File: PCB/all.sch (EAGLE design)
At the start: 122 parts, among them J1 ISP Programmer, J2 LIPO-BATTERY-CONNECTOR, J8 BL-HP20AUW2C, U1 ATTINY1634MLF20, U2 LM3671, U3 MPU-6050-1, U4 BQ51013B_RHL_20, U5 MCP73831, U6 CAT4139, U7 BQ51013B_RHL_20, U8 BQ51013B_RHL_20, U9 BQ51013B_RHL_20

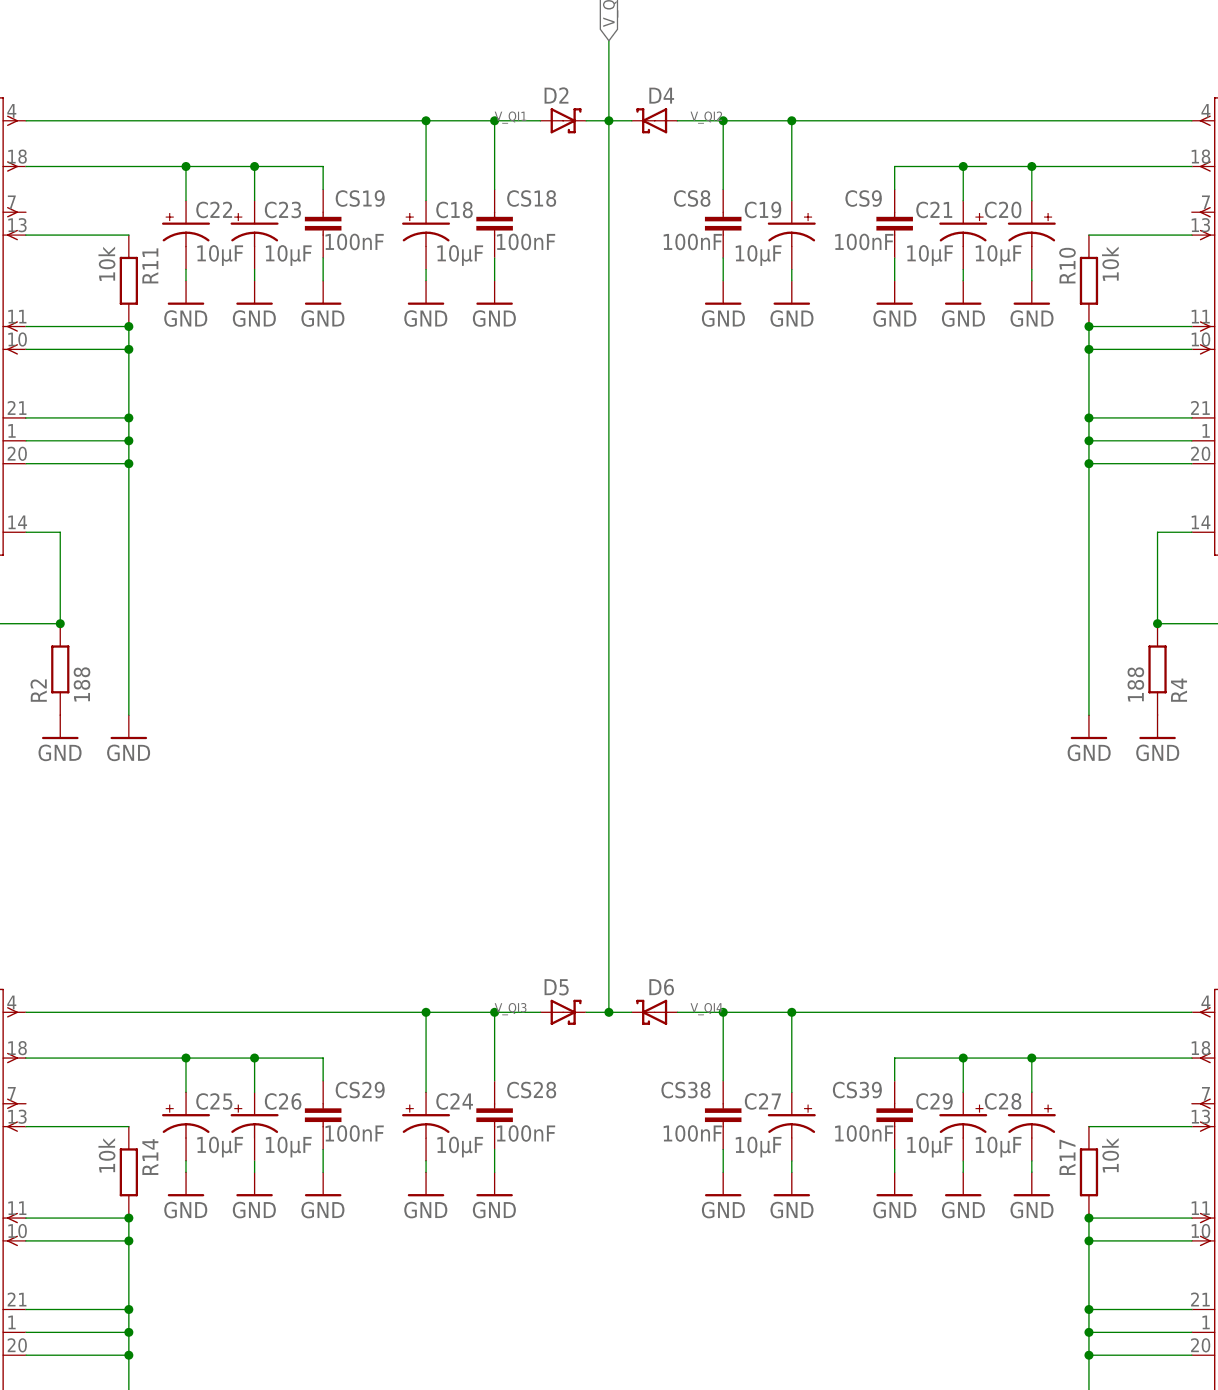
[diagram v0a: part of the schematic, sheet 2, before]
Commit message: rerouted Qi chargers and finished arrangements
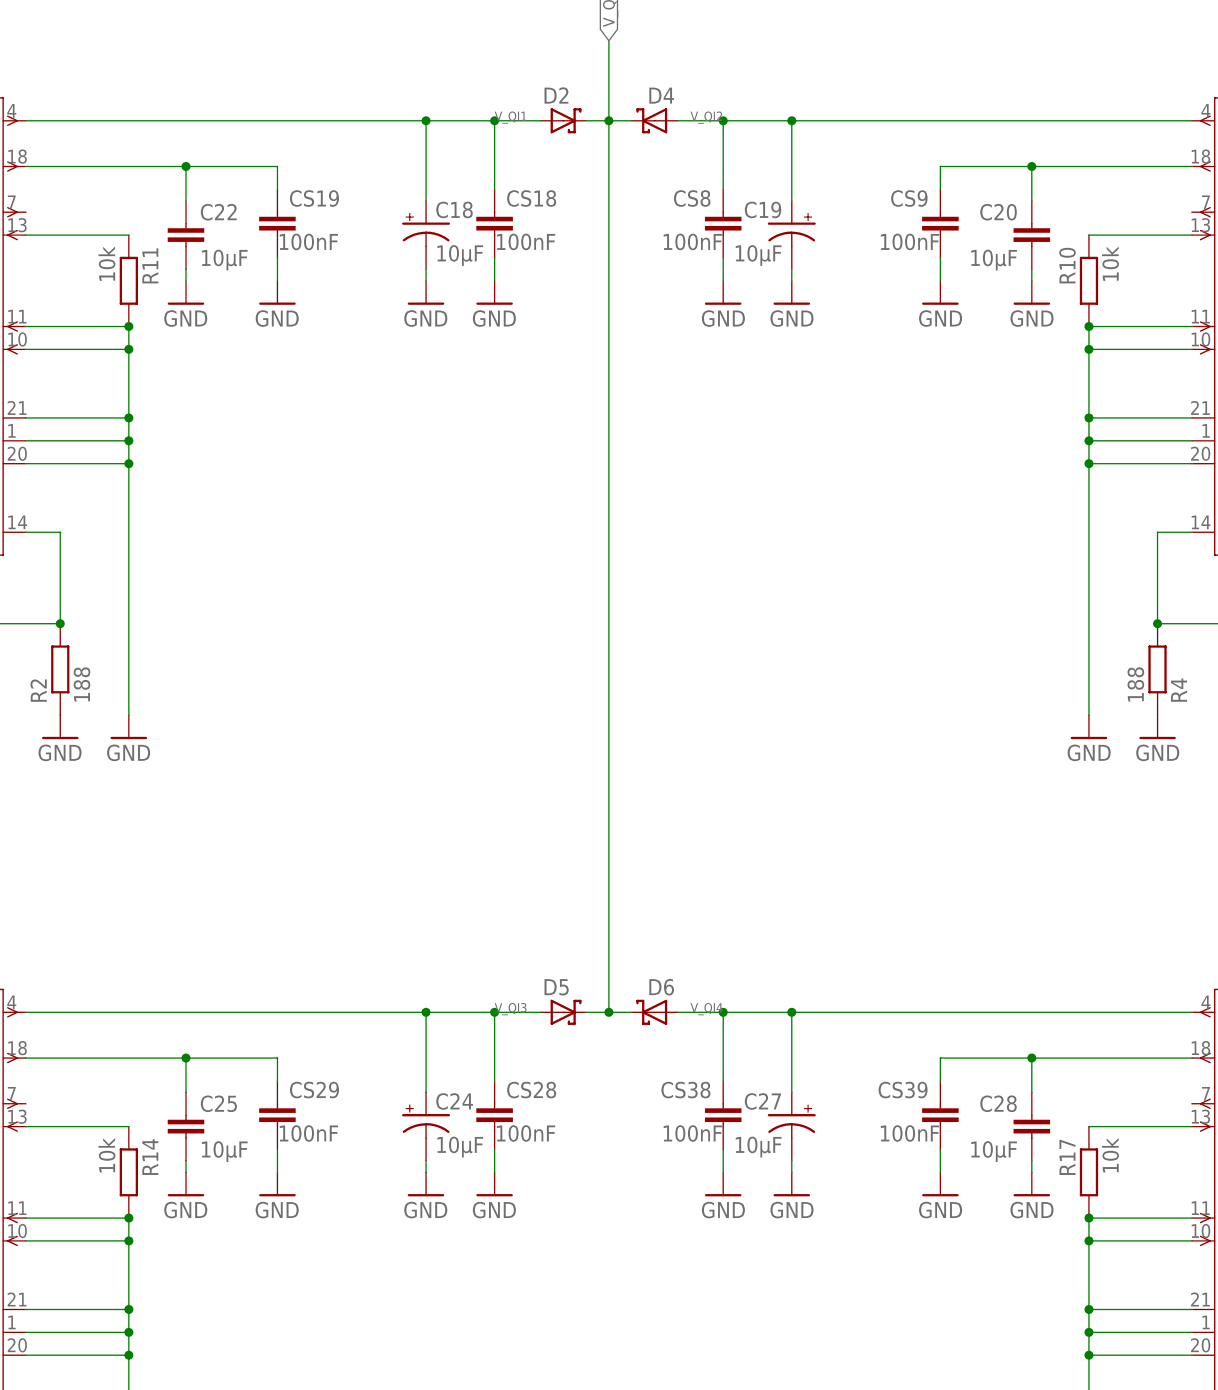
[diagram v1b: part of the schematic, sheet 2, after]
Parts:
- removed C21, C23, C26, C29: 10μF, SparkFun:CAP_POL1206
- C20, C22, C25, C28: device SparkFun:CAP_POL1206 -> rcl:C-EUC0603
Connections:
- net GND: now also C20.2, C22.2, C25.2, C28.2; no longer C20.-, C21.-, C22.-, C23.-, C25.-, C26.-, C28.-, C29.-
- net N$23: now also C20.1; no longer C20.+, C21.+
- net N$32: now also C22.1; no longer C22.+, C23.+
- net N$45: now also C25.1; no longer C25.+, C26.+
- net N$58: now also C28.1; no longer C28.+, C29.+
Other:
- note removed: "Battery charger: MCP73831 ---------------------- for charging current of 100 mA, R6 is 10k"
- moved on the sheet: CS19, CS29, CS39, CS9

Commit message: routing finished
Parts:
- C1, C17, C20, C22, C25, C28, C5, CP1, CP2, CP3, CP4, CP5, CP6, CP7, CP8, CS, CS1, CS10, CS11, CS12, CS13, CS14, CS15, CS16, CS17, CS19, CS2, CS20, CS21, CS22, CS23, CS24, CS25, CS26, CS27, CS28, CS29, CS3, CS30, CS31, CS32, CS33, CS34, CS35, CS36, CS37, CS38, CS39, CS4, CS5, CS6, CS7, CS8, CS9: device rcl:C-EUC0603 -> rcl:C-EUC0603K
- C10, C11, C12, C6, C7, C8, C9: device rcl:C-EUC0402 -> rcl:C-EUC0603K
- C13: device SparkFun:CAP0603-CAP -> rcl:C-EUC0603K
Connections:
- removed net VBAT: J2.+, U5.VBAT
- net 5V: now also J2.+
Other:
- moved on the sheet: C13

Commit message: DRC done
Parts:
- J3, J4, J5, J6: value (none) -> Qi coil
- J7: value (none) -> UART
- Q1, Q2: value (none) -> NPN
- R18: value (none) -> 1.8
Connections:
- removed net 5V: C1.1, C14.+, C8.1, J1.2, J2.+, JP2.2, L1.1, SJ2.3, U2.EN, U2.IN, U6.VIN
- new net +5V: C1.1, C14.+, C8.1, J1.2, J2.+, JP2.2, L1.1, SJ2.3, U2.EN, U2.IN, U5.VBAT, U6.VIN

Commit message: fabrication output generated
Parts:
- added FD1, FD2: FIDUCIAL1X2, SparkFun-Aesthetics:FIDUCIAL1X2
- SJ1, SJ2: value (none) -> JUMPER-PAD-3-2OF3_NC_BY_TRACE_SMALL; device SparkFun-Retired:SOLDERJUMPER_2WAYPASTE2&3 -> SparkFun-Passives:JUMPER-PAD-3-2OF3_NC_BY_TRACE_SMALL
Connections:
- net +5V: now also SJ2.1; no longer SJ2.3
- net N$3: now also SJ1.1; no longer SJ1.3
- net N$4: now also SJ1.3; no longer SJ1.1
- net N$64: now also SJ2.3; no longer SJ2.1
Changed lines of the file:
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@@
 <part name="R18" library="rcl" deviceset="R-EU_" device="R0603" value="1.8"/>
 <part name="GND3" library="SparkFun" deviceset="GND" device=""/>
-<part name="SJ1" library="SparkFun-Retired" deviceset="SOLDERJUMPER_2WAY" device="PASTE2&amp;3"/>
+<part name="SJ1" library="SparkFun-Passives" deviceset="JUMPER-PAD-3-2OF3_NC_BY_TRACE" device="_SMALL" value=""/>
 <part name="U6" library="pero_library" deviceset="CAT4139" device="" value="CAT4139"/>
 <part name="C1" library="rcl" deviceset="C-EU" device="C0603K" value="10μF"/>
@@
 <part name="GND29" library="SparkFun" deviceset="GND" device=""/>
 <part name="R20" library="resistor" deviceset="R-EU_" device="R0603" value="1k"/>
-<part name="SJ2" library="SparkFun-Retired" deviceset="SOLDERJUMPER_2WAY" device="PASTE2&amp;3"/>
+<part name="SJ2" library="SparkFun-Passives" deviceset="JUMPER-PAD-3-2OF3_NC_BY_TRACE" device="_SMALL" value=""/>
 <part name="FRAME3" library="frames" deviceset="A4L-LOC" device=""/>
 <part name="L2" library="SparkFun-Passives" deviceset="INDUCTOR" device="SDR0403-560KL" value="22uH"/>
@@
 <part name="P+5" library="supply1" deviceset="+5V" device=""/>
 <part name="U5" library="SparkFun-PowerIC" deviceset="MCP73831" device=""/>
+<part name="FD1" library="SparkFun-Aesthetics" deviceset="FIDUCIAL" device="1X2"/>
+<part name="FD2" library="SparkFun-Aesthetics" deviceset="FIDUCIAL" device="1X2"/>
 </parts>
 <sheets>
@@
 <instance part="R18" gate="G$1" x="226.06" y="76.2" rot="R90"/>
 <instance part="GND3" gate="1" x="226.06" y="66.04"/>
-<instance part="SJ1" gate="G$1" x="213.36" y="96.52"/>
+<instance part="SJ1" gate="G$1" x="213.36" y="96.52" rot="MR180"/>
 <instance part="U6" gate="G$1" x="185.42" y="127" smashed="yes">
 <attribute name="NAME" x="175.26" y="134.62" size="1.778" layer="95"/>
@@
 <instance part="GND29" gate="1" x="218.44" y="109.22"/>
 <instance part="R20" gate="G$1" x="208.28" y="121.92"/>
-<instance part="SJ2" gate="G$1" x="220.98" y="139.7" rot="R90"/>
+<instance part="SJ2" gate="G$1" x="220.98" y="139.7" smashed="yes" rot="MR90">
+<attribute name="NAME" x="220.98" y="142.621" size="1.778" layer="95" rot="MR0"/>
+<attribute name="VALUE" x="219.075" y="142.24" size="1.778" layer="96" rot="MR90"/>
+</instance>
 <instance part="FRAME3" gate="G$1" x="0" y="0"/>
 <instance part="L2" gate="G$1" x="130.81" y="153.67" smashed="yes" rot="R90">
 <attribute name="NAME" x="128.27" y="158.242" size="1.778" layer="95" rot="R180"/>
 </instance>
-<instance part="P+1" gate="1" x="92.71" y="158.75"/>
-<instance part="P+2" gate="1" x="226.06" y="144.78"/>
-<instance part="P+3" gate="1" x="162.56" y="144.526"/>
-<instance part="P+4" gate="1" x="162.56" y="65.786"/>
-<instance part="P+5" gate="1" x="101.6" y="121.92"/>
+<instance part="P+1" gate="1" x="92.71" y="158.75" smashed="yes">
+<attribute name="VALUE" x="95.25" y="161.29" size="1.778" layer="96" rot="R180"/>
+</instance>
+<instance part="P+2" gate="1" x="226.06" y="144.78" smashed="yes">
+<attribute name="VALUE" x="228.6" y="147.32" size="1.778" layer="96" rot="R180"/>
+</instance>
+<instance part="P+3" gate="1" x="162.56" y="144.526" smashed="yes">
+<attribute name="VALUE" x="165.354" y="147.32" size="1.778" layer="96" rot="R180"/>
+</instance>
+<instance part="P+4" gate="1" x="162.56" y="65.786" smashed="yes">
+<attribute name="VALUE" x="165.354" y="68.58" size="1.778" layer="96" rot="R180"/>
+</instance>
+<instance part="P+5" gate="1" x="101.6" y="121.92" smashed="yes">
+<attribute name="VALUE" x="104.14" y="124.46" size="1.778" layer="96" rot="R180"/>
+</instance>
 <instance part="U5" gate="G$1" x="46.99" y="151.13"/>
+<instance part="FD1" gate="G$1" x="215.9" y="43.18"/>
+<instance part="FD2" gate="G$1" x="226.06" y="43.18"/>
 </instances>
 <busses>
@@
 </segment>
 </net>
-<net name="N$3" class="0">
-<segment>
-<pinref part="Q1" gate="G$1" pin="B"/>
-<pinref part="Q2" gate="G$1" pin="C"/>
-<wire x1="220.98" y1="91.44" x2="213.36" y2="91.44" width="0.1524" layer="91"/>
-<wire x1="213.36" y1="91.44" x2="213.36" y2="88.9" width="0.1524" layer="91"/>
-<pinref part="SJ1" gate="G$1" pin="3"/>
-<junction x="213.36" y="91.44"/>
-</segment>
-</net>
 <net name="N$63" class="0">
 <segment>
@@
 <wire x1="208.28" y1="139.7" x2="210.82" y2="139.7" width="0.1524" layer="91"/>
 <pinref part="C17" gate="G$1" pin="1"/>
-<pinref part="SJ2" gate="G$1" pin="1"/>
+<pinref part="SJ2" gate="G$1" pin="3"/>
 <wire x1="210.82" y1="139.7" x2="215.9" y2="139.7" width="0.1524" layer="91"/>
 <junction x="210.82" y="139.7"/>
@@
 <pinref part="U6" gate="G$1" pin="SHDN"/>
 <wire x1="170.18" y1="121.92" x2="170.18" y2="101.6" width="0.1524" layer="91"/>
-<pinref part="SJ1" gate="G$1" pin="1"/>
+<pinref part="SJ1" gate="G$1" pin="3"/>
 <wire x1="170.18" y1="101.6" x2="213.36" y2="101.6" width="0.1524" layer="91"/>
 </segment>
@@
 </segment>
 <segment>
-<pinref part="SJ2" gate="G$1" pin="3"/>
-<wire x1="226.06" y1="139.7" x2="226.06" y2="142.24" width="0.1524" layer="91"/>
-<pinref part="P+2" gate="1" pin="+5V"/>
-</segment>
-<segment>
 <pinref part="C1" gate="G$1" pin="1"/>
 <wire x1="162.56" y1="129.54" x2="162.56" y2="139.7" width="0.1524" layer="91"/>
@@
 <pinref part="P+5" gate="1" pin="+5V"/>
 </segment>
-</net>
+<segment>
+<pinref part="SJ2" gate="G$1" pin="1"/>
+<pinref part="P+2" gate="1" pin="+5V"/>
+<wire x1="226.06" y1="139.7" x2="226.06" y2="142.24" width="0.1524" layer="91"/>
+</segment>
+</net>
+<net name="N$3" class="0">
+<segment>
+<pinref part="SJ1" gate="G$1" pin="1"/>
+<pinref part="Q2" gate="G$1" pin="C"/>
+<wire x1="213.36" y1="91.44" x2="213.36" y2="88.9" width="0.1524" layer="91"/>
+<pinref part="Q1" gate="G$1" pin="B"/>
+<wire x1="220.98" y1="91.44" x2="213.36" y2="91.44" width="0.1524" layer="91"/>
+<junction x="213.36" y="91.44"/>
+</segment>
+</net>

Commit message: going back to 32u4
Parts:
- removed J7: UART, SparkFun-Connectors:M02PTH
- removed R1: 10k, rcl:R-EU_R0603
- added C2: 1µF, rcl:C-EUC0603
- added C23, C3: 18p, rcl:C-EUC0603
- added F2: PTC0603, SparkFun-PowerIC:PTC0603
- added Q3: 8MHz, pero_library:QUARTZ-CRYSTAL-8MHZQC6CB8.00000F18B23R
- added R21: 10k, rcl:R-EU_R0603
- added R23, R24: 22, rcl:R-EU_R0603
- added S1: Reset, pero_library:SWITCH-BUTTON-SKSGAAE010
- J1: value ISP Programmer -> micro USB; device SparkFun:AVR_SPI_PRG_6PTH -> SparkFun-Connectors:USB_MICROB_PLUGCONN-11752
- L2: value 22uH -> 2.2uH
- U1: value ATTINY1634MLF20 -> ATMEGA32U4QFN; device attiny1634:ATTINY1634MLF20 -> SparkFun-DigitalIC:ATMEGA32U4QFN
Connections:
- removed net MISO: J1.1, U1.ADC7/MISO/TXD1/DO/PB2
- removed net RX: J7.1, U1.PA7/RXD0/ADC4
- removed net TX: J7.2, U1.PB0/TXD0/ADC5
- new net N$71: C23.2, Q3.2, U1.XTAL1
- new net N$72: C3.2, Q3.1, U1.XTAL2
- new net N$73: F2.1, J1.VCC
- new net N$74: J1.D+, R23.1
- new net N$78: J1.D-, R24.1
- new net N$80: R23.2, U1.D+
- new net N$81: R24.2, U1.D-
- new net VUSB: F2.2, U1.VBUS
- net +5V: no longer J1.2
- net 3.3V: now also C2.1, R21.2, U1.AVCC@24, U1.AVCC@44, U1.UCAP, U1.VCC@14, U1.VCC@34; no longer R1.2, U1.VCC
- net GND: now also C2.2, C23.1, C3.1, J1.GND, S1.1, U1.GND@15, U1.GND@23, U1.GND@35, U1.GND@43, U1.UGND; no longer J1.6, U1.GND
- net PWM: no longer U1.ADC9/OC0A/XCK0/PC0
- net RGB: no longer U1.PA6/ADC3/OC1B
- net RST: now also R21.1, S1.2, U1.!RESET; no longer J1.5, R1.1, U1.-RESET/PC3
- net SCL: now also U1.PD0(SCL); no longer J1.3, U1.ADC10/SCL/USCK/XCK1/PC1
- net SDA: now also U1.PD1(SDA); no longer J1.4, U1.RXD1/ADC6/DI/SDA/MOSI/PB1
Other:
- moved on the sheet: C1, C10, C11, C12, C13, C14, C15, C17, C5, C6, C7, C8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

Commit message: started routing with 32u4
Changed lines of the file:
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@@
 <setting verticaltext="up"/>
 </settings>
-<grid distance="0.1" unitdist="inch" unit="inch" style="lines" multiple="1" display="yes" altdistance="0.01" altunitdist="inch" altunit="inch"/>
+<grid distance="0.1" unitdist="inch" unit="inch" style="lines" multiple="1" display="no" altdistance="0.01" altunitdist="inch" altunit="inch"/>
 <layers>
 <layer number="1" name="Top" color="4" fill="1" visible="no" active="no"/>
@@
 </instance>
 <instance part="C23" gate="G$1" x="73.66" y="68.58" smashed="yes" rot="R90">
-<attribute name="NAME" x="80.01" y="73.025" size="1.778" layer="95" rot="R180"/>
+<attribute name="NAME" x="73.66" y="70.993" size="1.778" layer="95" rot="R180"/>
 <attribute name="VALUE" x="80.01" y="70.739" size="1.778" layer="96" rot="R180"/>
 </instance>
@@
 <segment>
 <pinref part="F2" gate="G$1" pin="2"/>
-<wire x1="50.8" y1="73.66" x2="53.34" y2="73.66" width="0.1524" layer="91"/>
-<label x="53.34" y="73.66" size="1.016" layer="95" xref="yes"/>
-<label x="83.82" y="88.9" size="1.016" layer="95" rot="R180" xref="yes"/>
-</segment>
-<segment>
+<label x="83.82" y="88.9" size="1.016" layer="95"/>
 <pinref part="U1" gate="G$1" pin="VBUS"/>
 <wire x1="83.82" y1="88.9" x2="91.44" y2="88.9" width="0.1524" layer="91"/>
-</segment>
-</net>
+<wire x1="50.8" y1="73.66" x2="83.82" y2="73.66" width="0.1524" layer="91"/>
+<wire x1="83.82" y1="73.66" x2="83.82" y2="88.9" width="0.1524" layer="91"/>
+</segment>
+</net>
